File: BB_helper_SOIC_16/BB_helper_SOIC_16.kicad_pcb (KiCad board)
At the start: 2 copper layers, 15.5 x 20.6 mm, 3 parts, among them J1 Conn_01x08_PinHeader, J2 Conn_01x08_PinHeader, U1 SSI2164

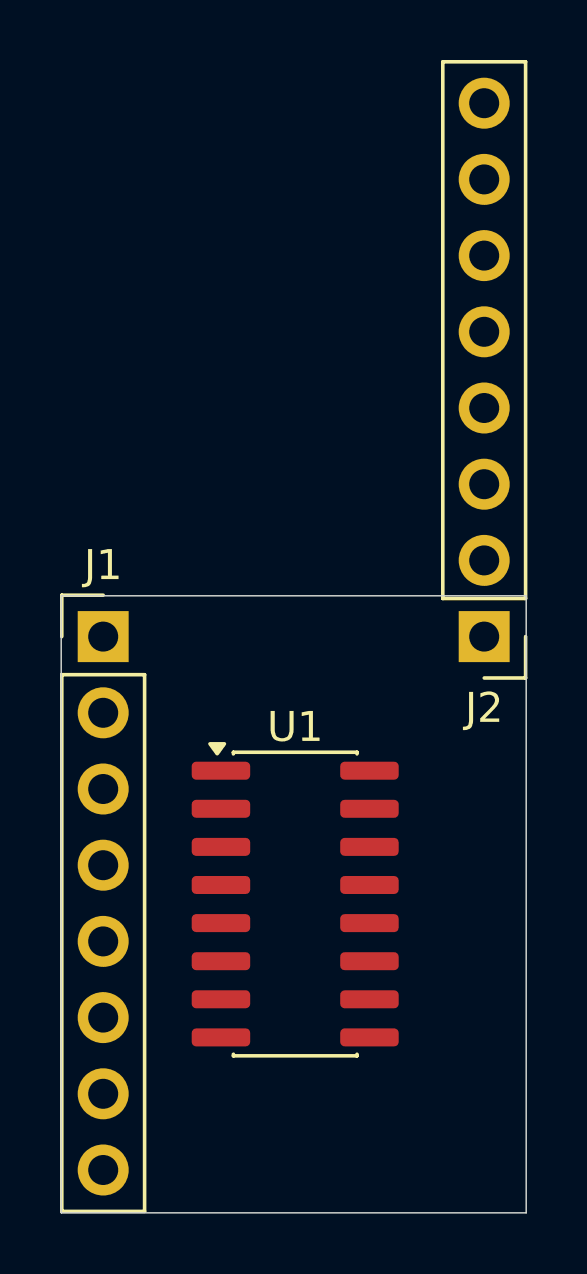
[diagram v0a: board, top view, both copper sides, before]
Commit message: Designed SOIC 16 and SSOP 10 DIP converters
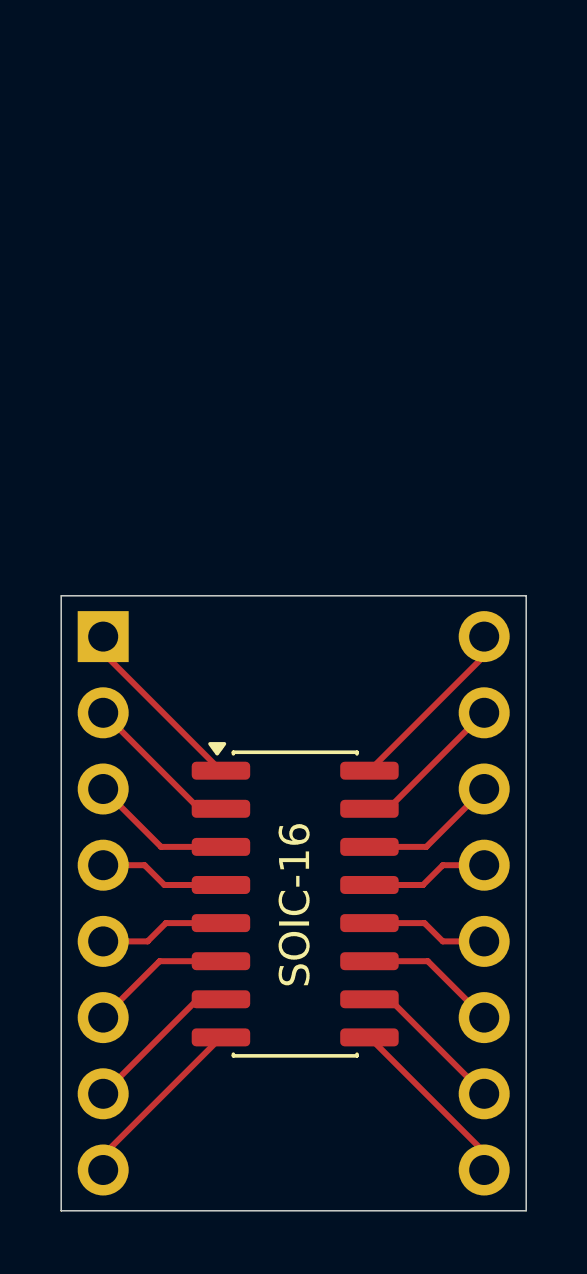
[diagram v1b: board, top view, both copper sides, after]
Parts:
- J1, J2: moved to B.Cu
- moved J2 17.8 mm to (66.3, 49.1), turned to 0 degrees
- turned J1 to 180 degrees
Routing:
- net Net-(J1A-Pin_1): track 0.00 -> 6.10 mm
- net Net-(J2H-Pin_8): track 0.00 -> 6.05 mm
- net Net-(J1H-Pin_8): track 0.00 -> 6.05 mm
- net Net-(J2A-Pin_1): track 0.00 -> 6.00 mm
- net Net-(J1B-Pin_2): track 0.00 -> 5.25 mm
- net Net-(J1G-Pin_7): track 0.00 -> 5.23 mm
- net Net-(J2G-Pin_7): track 0.00 -> 5.15 mm
- net Net-(J2B-Pin_2): track 0.00 -> 5.13 mm
- net Net-(J1C-Pin_3): track 0.00 -> 4.72 mm
- net Net-(J1F-Pin_6): track 0.00 -> 4.70 mm
- net Net-(J2F-Pin_6): track 0.00 -> 4.62 mm
- net Net-(J2C-Pin_3): track 0.00 -> 4.60 mm
- net Net-(J1D-Pin_4): track 0.00 -> 4.20 mm
- net Net-(J1E-Pin_5): track 0.00 -> 4.18 mm
- net Net-(J2E-Pin_5): track 0.00 -> 4.10 mm
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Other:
- board size 15.5 x 20.6 mm -> 15.5 x 20.5 mm
- board text added: "SOIC-16"
